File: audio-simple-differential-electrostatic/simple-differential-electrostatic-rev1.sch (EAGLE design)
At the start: 81 parts, among them IC1 LT1115, IC2 LT1115, IC3 LT1115, IC4 LT1115, IC5 LM7915, IC6 LM7815, IC7 LM317T, IC8 LM317T, J1 LOUT, J2 VIN_PLATE, J3 ROUT, X1 LIN, X2 VIN_OPAMP, X3 RIN, X4 VIN_HEATER

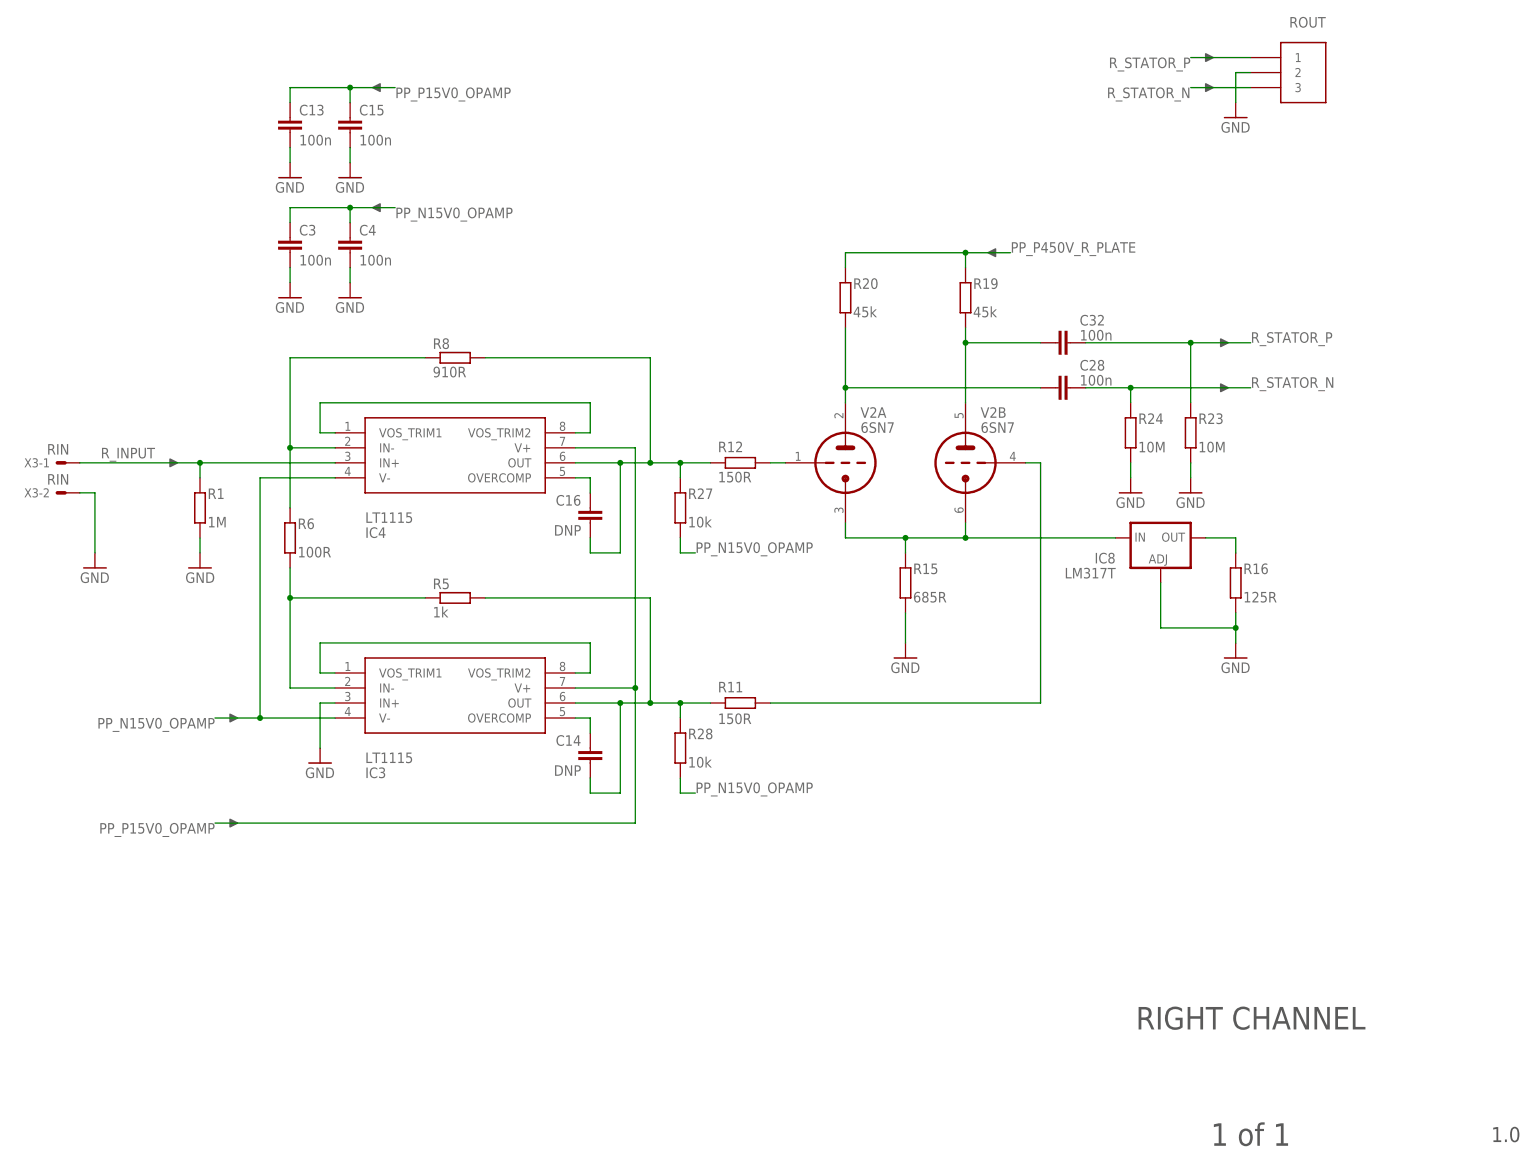
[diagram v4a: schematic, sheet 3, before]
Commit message: Removed incorrect offset nulling shorts, ran renumber with new pulldown resistors
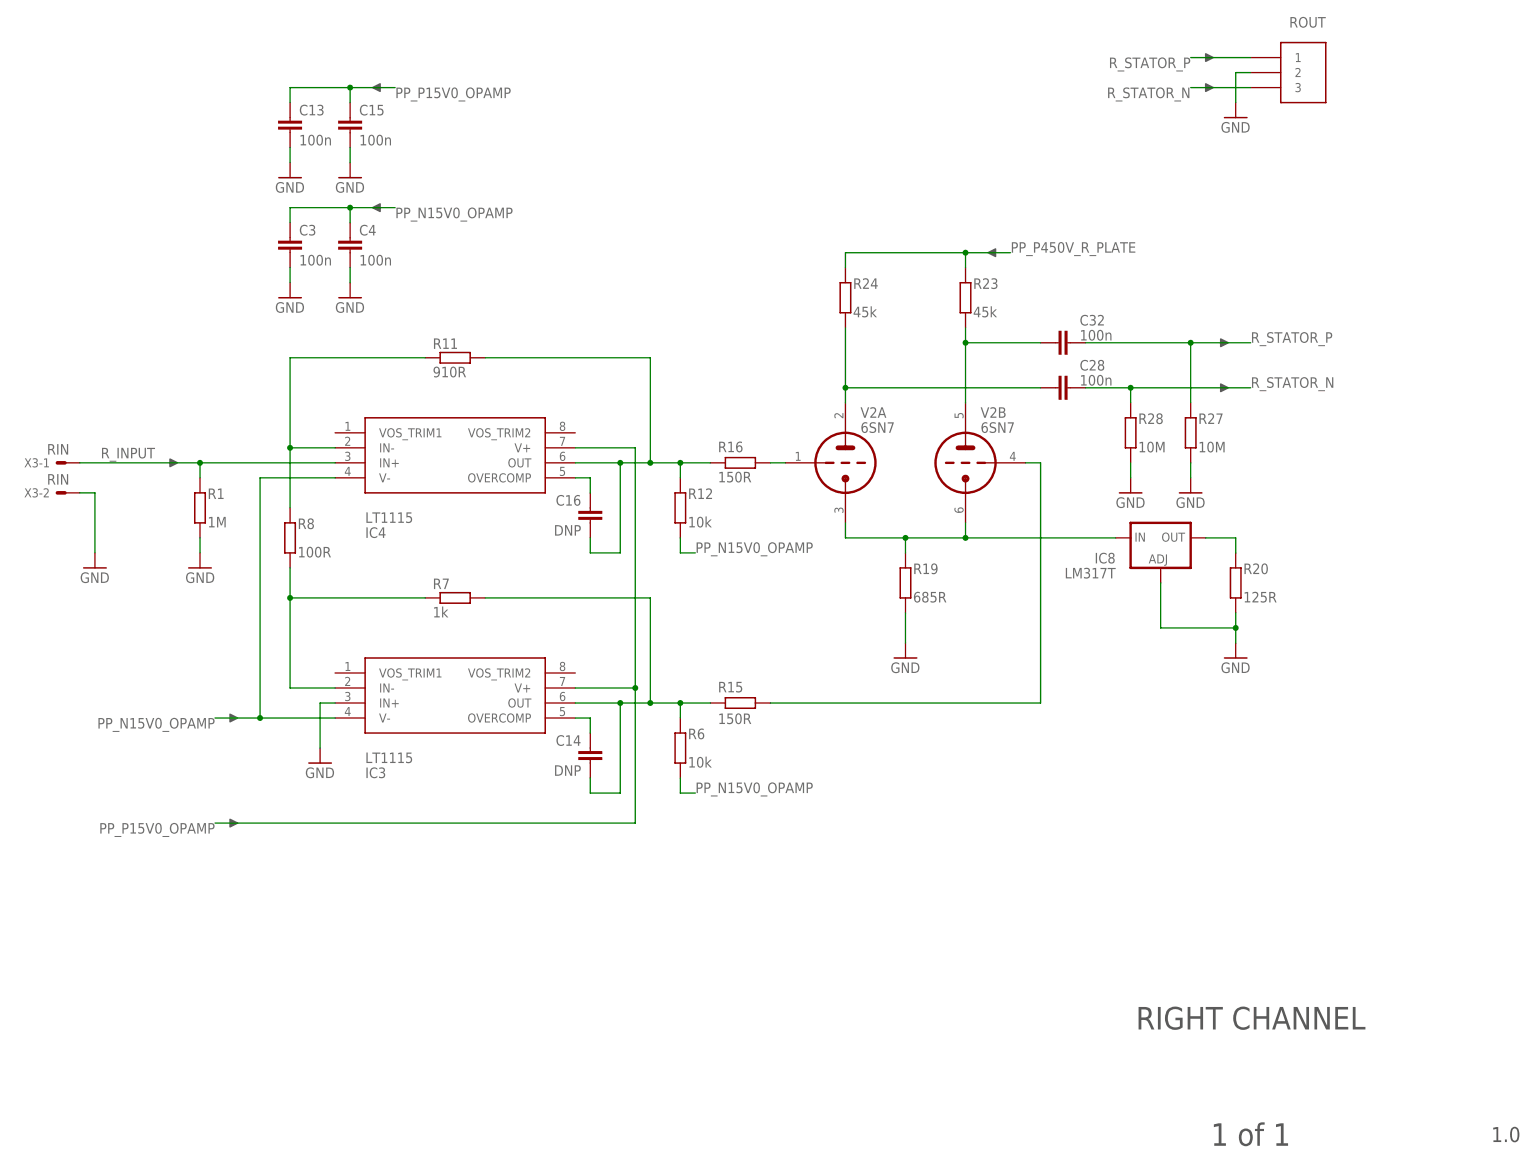
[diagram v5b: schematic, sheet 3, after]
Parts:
- R10, R12: value 150R -> 10k
- R11, R9: value 150R -> 910R
- R13, R16: value 125R -> 150R
- R14, R15: value 685R -> 150R
- R17, R20: value 45k -> 125R; device rcl:R-EU_0613/15 -> rcl:R-EU_0309/10
- R18, R19: value 45k -> 685R; device rcl:R-EU_0613/15 -> rcl:R-EU_0309/10
- R21, R22, R23, R24: value 10M -> 45k; device rcl:R-EU_0309/10 -> rcl:R-EU_0613/15
- R25, R26, R27, R28: value 10k -> 10M
- R3: value 1k -> 10k
- R4: value 100R -> 1k
- R5: value 1k -> 100R
- R6: value 100R -> 10k
- R7: value 910R -> 1k
- R8: value 910R -> 100R
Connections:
- removed net N$11: IC3.VOS_TRIM1, IC3.VOS_TRIM2
- removed net N$18: IC2.VOS_TRIM1, IC2.VOS_TRIM2
- removed net N$20: IC1.VOS_TRIM1, IC1.VOS_TRIM2
- removed net N$9: IC4.VOS_TRIM1, IC4.VOS_TRIM2
- net GND: now also R17.1, R18.1, R19.1, R20.1, R25.1, R26.1, R27.1, R28.1; no longer R13.1, R14.1, R15.1, R16.1, R21.1, R22.1, R23.1, R24.1
- net L_STATOR_N: now also R26.2; no longer R22.2
- net L_STATOR_P: now also R25.2; no longer R21.2
- net N$1: now also R19.2; no longer R15.2
- net N$10: now also R11.1; no longer R6.1
- net N$12: now also R21.1; no longer R17.1
- net N$13: now also R7.1, R8.2; no longer R5.1, R6.2
- net N$14: now also R15.2, R6.2, R7.2; no longer R11.2, R28.2, R5.2
- net N$15: now also R13.1; no longer R9.1
- net N$16: now also R14.1; no longer R10.1
- net N$17: now also R14.2, R9.2; no longer R25.2, R7.2
- net N$19: now also R5.1, R9.1; no longer R4.1, R7.1
- net N$2: now also R24.1; no longer R20.1
- net N$21: now also R4.1, R5.2; no longer R3.1, R4.2
- net N$22: now also R13.2, R4.2; no longer R26.2, R9.2
- net N$25: now also R20.2; no longer R16.2
- net N$3: now also R23.1; no longer R19.1
- net N$36: now also R17.2; no longer R13.2
- net N$4: now also R11.2, R16.2; no longer R27.2, R8.2
- net N$5: now also R18.2; no longer R14.2
- net N$6: now also R22.1; no longer R18.1
- net N$7: now also R15.1; no longer R11.1
- net N$8: now also R16.1; no longer R12.1
- net PP_N15V0_OPAMP: now also R10.1, R12.1, R3.1, R6.1; no longer R25.1, R26.1, R27.1, R28.1
- net PP_P450V_L_PLATE: now also R21.2, R22.2; no longer R17.2, R18.2
- net PP_P450V_R_PLATE: now also R23.2, R24.2; no longer R19.2, R20.2
- net R_STATOR_N: now also R28.2; no longer R24.2
- net R_STATOR_P: now also R27.2; no longer R23.2
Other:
- moved on the sheet: R10, R11, R12, R13, R14, R15, R16, R17, R18, R19, R20, R21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

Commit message: t
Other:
- note added: "1 of 2"
- note added: "SIMPLE DIFFERENTIAL ELECTROSTATIC AMPLIFIER BOARD"
- note removed: "1 of 1"
- note removed: "LINEAR ACTIVE SPAD QUENCHING CIRCUIT"
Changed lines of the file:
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@@
 <text x="223.52" y="30.48" size="3.81" layer="97" font="vector" align="center">TABLE OF CONTENTS</text>
 <text x="266.7" y="10.795" size="2.54" layer="97" font="vector" align="center">1.0</text>
-<text x="223.52" y="10.795" size="3.81" layer="97" font="vector" align="center">1 of 1</text>
-<text x="139.7" y="195.58" size="5.08" layer="97" font="vector" align="center">LINEAR ACTIVE SPAD QUENCHING CIRCUIT</text>
+<text x="223.52" y="10.795" size="3.81" layer="97" font="vector" align="center">1 of 2</text>
+<text x="139.7" y="195.58" size="5.08" layer="97" font="vector" align="center">SIMPLE DIFFERENTIAL ELECTROSTATIC AMPLIFIER BOARD</text>
 <text x="73.66" y="162.56" size="3.81" layer="97" font="vector" align="center">SHEET</text>
 <text x="142.24" y="162.56" size="3.81" layer="97" font="vector" align="center">CONTENTS</text>
@@
 <text x="223.52" y="27.94" size="3.81" layer="97" font="vector" align="center">POWER SUPPLIES</text>
 <text x="266.7" y="8.255" size="2.54" layer="97" font="vector" align="center">1.0</text>
-<text x="223.52" y="8.255" size="3.81" layer="97" font="vector" align="center">1 of 1</text>
+<text x="223.52" y="8.255" size="3.81" layer="97" font="vector" align="center">1 of 2</text>
 </plain>
 <instances>
@@
 <text x="223.52" y="27.94" size="3.81" layer="97" font="vector" align="center">RIGHT CHANNEL</text>
 <text x="266.7" y="8.255" size="2.54" layer="97" font="vector" align="center">1.0</text>
-<text x="223.52" y="8.255" size="3.81" layer="97" font="vector" align="center">1 of 1</text>
+<text x="223.52" y="8.255" size="3.81" layer="97" font="vector" align="center">1 of 2</text>
 </plain>
 <instances>
@@
 <text x="223.52" y="27.94" size="3.81" layer="97" font="vector" align="center">LEFT CHANNEL</text>
 <text x="266.7" y="8.255" size="2.54" layer="97" font="vector" align="center">1.0</text>
-<text x="223.52" y="8.255" size="3.81" layer="97" font="vector" align="center">1 of 1</text>
+<text x="223.52" y="8.255" size="3.81" layer="97" font="vector" align="center">1 of 2</text>
 </plain>
 <instances>
